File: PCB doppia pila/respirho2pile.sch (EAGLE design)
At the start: 30 parts, among them J1 HEADERLESS, SW1 EG1213, SW2 KSS231GLFS, U1 ICM-20948, U2 AP2127K-1.8V, X1 32,768kHz

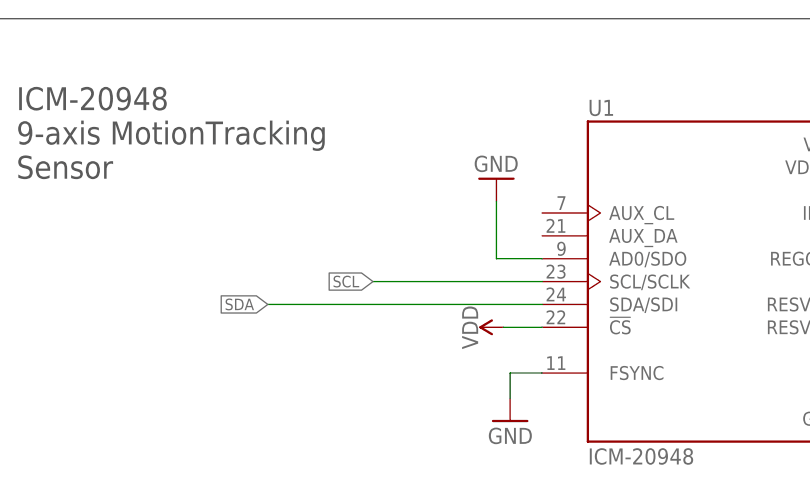
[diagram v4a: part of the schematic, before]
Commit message: aggiunte resistenze di pull up i2c
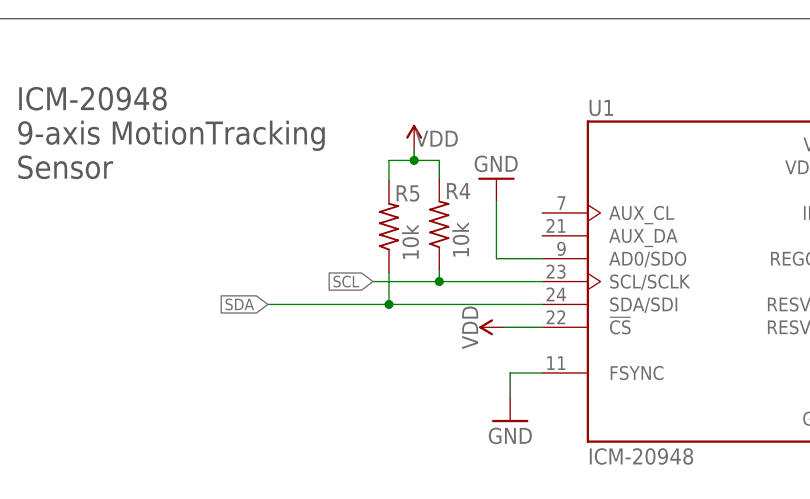
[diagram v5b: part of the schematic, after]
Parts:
- added R4, R5: 10k, rcl:R-US_R0402
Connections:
- net SCL: now also R4.1
- net SDA: now also R5.1
- net VDD: now also R4.2, R5.2
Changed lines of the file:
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@@
 <part name="C9" library="rcl" library_urn="urn:adsk.eagle:library:334" deviceset="C-EU" device="C0603" package3d_urn="urn:adsk.eagle:package:23616/2" value="1u"/>
 <part name="GND8" library="supply1" deviceset="GND" device=""/>
+<part name="R4" library="rcl" library_urn="urn:adsk.eagle:library:334" deviceset="R-US_" device="R0402" package3d_urn="urn:adsk.eagle:package:23547/3" value="10k"/>
+<part name="R5" library="rcl" library_urn="urn:adsk.eagle:library:334" deviceset="R-US_" device="R0402" package3d_urn="urn:adsk.eagle:package:23547/3" value="10k"/>
+<part name="SUPPLY4" library="SparkFun-PowerSymbols" library_urn="urn:adsk.eagle:library:530" deviceset="VDD" device=""/>
 </parts>
 <sheets>
@@
 <attribute name="VALUE" x="-135.636" y="60.96" size="1.778" layer="96" rot="MR0"/>
 </instance>
+<instance part="R4" gate="G$1" x="-130.81" y="165.1" smashed="yes" rot="R90">
+<attribute name="NAME" x="-127.254" y="169.6974" size="1.778" layer="95" rot="R180"/>
+<attribute name="VALUE" x="-127.508" y="161.29" size="1.778" layer="96" rot="R90"/>
+</instance>
+<instance part="R5" gate="G$1" x="-136.398" y="164.846" smashed="yes" rot="R90">
+<attribute name="NAME" x="-132.842" y="169.4434" size="1.778" layer="95" rot="R180"/>
+<attribute name="VALUE" x="-133.096" y="161.036" size="1.778" layer="96" rot="R90"/>
+</instance>
+<instance part="SUPPLY4" gate="VDD" x="-133.604" y="173.482" smashed="yes">
+<attribute name="VALUE" x="-131.064" y="173.736" size="1.778" layer="96" align="bottom-center"/>
+</instance>
 </instances>
 <busses>
@@
 <pinref part="C5" gate="G$1" pin="2"/>
 </segment>
+<segment>
+<pinref part="R5" gate="G$1" pin="2"/>
+<wire x1="-136.398" y1="169.926" x2="-136.398" y2="172.212" width="0.1524" layer="91"/>
+<wire x1="-136.398" y1="172.212" x2="-133.604" y2="172.212" width="0.1524" layer="91"/>
+<pinref part="R4" gate="G$1" pin="2"/>
+<wire x1="-133.604" y1="172.212" x2="-130.81" y2="172.212" width="0.1524" layer="91"/>
+<wire x1="-130.81" y1="172.212" x2="-130.81" y2="170.18" width="0.1524" layer="91"/>
+<pinref part="SUPPLY4" gate="VDD" pin="VDD"/>
+<wire x1="-133.604" y1="173.482" x2="-133.604" y2="172.212" width="0.1524" layer="91"/>
+<junction x="-133.604" y="172.212"/>
+</segment>
 </net>
 <net name="P0.24" class="0">
@@
 <segment>
 <pinref part="U1" gate="G$1" pin="SCL/SCLK"/>
-<wire x1="-119.38" y1="158.75" x2="-138.176" y2="158.75" width="0.1524" layer="91"/>
+<wire x1="-119.38" y1="158.75" x2="-130.81" y2="158.75" width="0.1524" layer="91"/>
 <label x="-138.176" y="158.75" size="1.27" layer="95" rot="R180" xref="yes"/>
+<pinref part="R4" gate="G$1" pin="1"/>
+<wire x1="-130.81" y1="158.75" x2="-138.176" y2="158.75" width="0.1524" layer="91"/>
+<wire x1="-130.81" y1="160.02" x2="-130.81" y2="158.75" width="0.1524" layer="91"/>
+<junction x="-130.81" y="158.75"/>
 </segment>
 <segment>
@@
 <segment>
 <pinref part="U1" gate="G$1" pin="SDA/SDI"/>
-<wire x1="-149.86" y1="156.21" x2="-119.38" y2="156.21" width="0.1524" layer="91"/>
+<wire x1="-149.86" y1="156.21" x2="-136.398" y2="156.21" width="0.1524" layer="91"/>
 <label x="-149.86" y="156.21" size="1.27" layer="95" rot="R180" xref="yes"/>
-</segment>
-<segment>
+<pinref part="R5" gate="G$1" pin="1"/>
+<wire x1="-136.398" y1="156.21" x2="-119.38" y2="156.21" width="0.1524" layer="91"/>
+<wire x1="-136.398" y1="159.766" x2="-136.398" y2="156.21" width="0.1524" layer="91"/>
+<junction x="-136.398" y="156.21"/>
+</segment>
+<segment>
